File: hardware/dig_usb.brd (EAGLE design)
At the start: 146.1 x 102.6 mm, 182 parts, among them IC101 AT90USB1287-AU, IC102 74HC166D, IC103 MAX487CSA, IC202 DS1337S, IC301 LTV-356T, IC302 LTV-356T, IC303 LTV-356T, IC304 LTV-356T, IC305 LTV-356T, IC306 LTV-356T, IC307 LTV-356T, IC308 LTV-356T, K401 S202S02, K402 S202S02, K403 S202S02, K404 S202S02, K405 S202S02, K406 S202S02, K407 S202S02, K408 S202S02, Q1 16MHz, Q201 32,768kHz, T301 BCR191, T302 BCR191, T303 BCR191, T304 BCR191, T305 BCR191, T306 BCR191, T307 BCR191, T308 BCR191, X1 AKL_249-08, X102 ISP, X2 AKL_249-08, X3 AKL_230-02, X301 RIA-73-02, X302 RIA-73-02, X303 RIA-73-02, X304 RIA-73-02, X305 RIA-73-02, X4 AKL_230-02, X401 RIA-73-02, X402 RIA-73-02, X403 RIA-73-02, X404 RIA-73-02, X405 RIA-73-02, X406 RIA-73-02, X407 RIA-73-02, X5 AKL_230-04

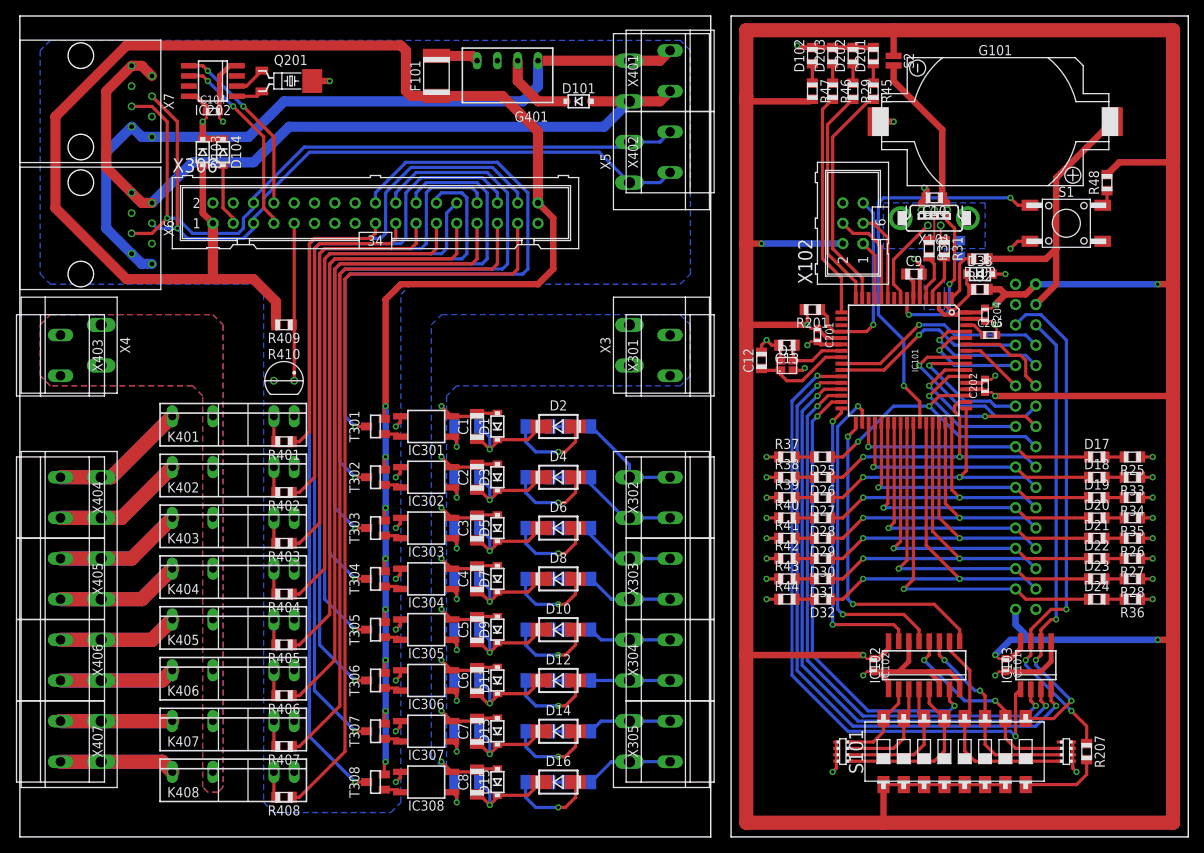
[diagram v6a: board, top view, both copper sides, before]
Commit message: dig_usb: Bauteile neu nummeriert und Plan etwas verschönert
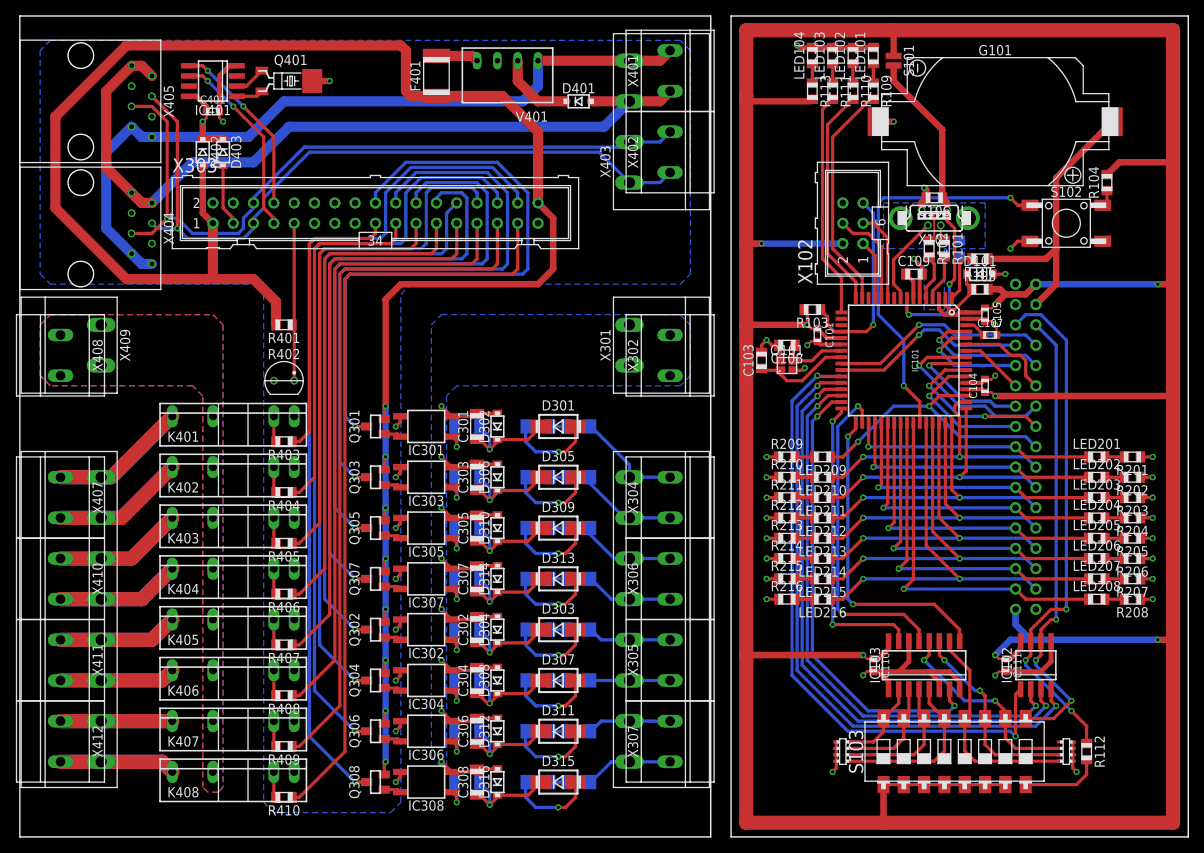
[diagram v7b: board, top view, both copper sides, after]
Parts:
- removed C11: 100nF, passiv:CHIP_0805
- removed C201, C202: 100nF, passiv:CHIP_0603
- removed D33: MMSZ5222BT1, diode:SOD123
- removed R25, R28, R36, R37: 1,5kΩ, passiv:CHIP_0805
- removed R30: 22Ω, passiv:CHIP_0805
- removed S2: (no value), schalter:JUMPER2
- removed X1: AKL_249-08, anschluss:AKL_230-08
- removed X3: AKL_230-02, anschluss:AKL_230-02
- removed X5: AKL_230-04, anschluss:AKL_230-04
- removed X6, X7: (no value), stecker:C-BMJ-0102
- added C110, C111, C401: 100nF, passiv:CHIP_0603
- added D401: SD103, diode:SOD123
- added R103: 10k, passiv:CHIP_0805
- added R106: 1MΩ, passiv:CHIP_0805
- added R107, R108: 22kΩ, widerstandsnetzwerk:1206
- added R112: 120Ω, passiv:CHIP_0805
- added S103: (no value), schalter:DIP08_SMD
- added X307, X408, X410, X411, X412: (no value), anschluss:RIA-73-02
- C102: device passiv:CHIP_0603 -> passiv:CHIP_0805
- D101: value SD103 -> MMSZ5222BT1
- D301, D303, D305, D307, D309, D311, D313, D315: value (none) -> MRA4007
- IC102: value 74HC166D -> MAX487CSA; device ic-logik:SOP16_127 -> ic-wandler:SOP08_127
- IC103: value MAX487CSA -> 74HC166D; device ic-wandler:SOP08_127 -> ic-logik:SOP16_127
- R102: value 1MΩ -> 22Ω
- R201: value 10k -> 1,5kΩ
- R207: value 120Ω -> 1,5kΩ
- R208, R209: value 22kΩ -> 1,5kΩ; device widerstandsnetzwerk:1206 -> passiv:CHIP_0805
- R401: value 470Ω -> 3,3kΩ
- R402: value 470Ω -> KTY81-210; device passiv:CHIP_0805 -> sensor:TO92
- R409: value 3,3kΩ -> 470Ω
- R410: value KTY81-210 -> 470Ω; device sensor:TO92 -> passiv:CHIP_0805
- S101: device schalter:DIP08_SMD -> schalter:JUMPER2
- X301: value RIA-73-02 -> (none); device anschluss:RIA-73-02 -> anschluss:AKL_230-02
- X302, X304, X305, X401, X402, X407: value RIA-73-02 -> (none)
- X303: value RIA-73-02 -> (none); device anschluss:RIA-73-02 -> anschluss:WS34V
- X306: device anschluss:WS34V -> anschluss:RIA-73-02
- X308: value AKL_249-08 -> (none)
- X403: value RIA-73-02 -> (none); device anschluss:RIA-73-02 -> anschluss:AKL_230-04
- X404, X405: value RIA-73-02 -> (none); device anschluss:RIA-73-02 -> stecker:C-BMJ-0102
- X406: value RIA-73-02 -> (none); device anschluss:RIA-73-02 -> anschluss:AKL_230-08
- X409: value AKL_230-02 -> (none)
- moved C104 102.4 mm to (120.7, 55.9), turned to 90 degrees
- moved S101 86.7 mm to (109.2, 96.5), turned to 270 degrees
- moved X403 76.9 mm to (76.2, 88.9), turned to 90 degrees
- moved X405 59.7 mm to (7.62, 91.4)
- moved X303 58.7 mm to (44.5, 77.5), turned to 0 degrees
- moved X306 58.7 mm to (81.3, 31.8), turned to 90 degrees
- moved D101 54.6 mm to (120.0, 69.8)
- moved C102 53.2 mm to (117.5, 73.0), flipped to the bottom
- moved R409 52.7 mm to (33.0, 10.8)
- moved R410 52.1 mm to (33.0, 4.45), turned to 180 degrees
- moved R209 50.8 mm to (95.9, 47.0), turned to 0 degrees
- moved C101 47.5 mm to (99.7, 62.2)
- moved R201 44.0 mm to (139.1, 47.0)
- moved R208 40.9 mm to (139.1, 29.2), turned to 180 degrees
- moved X404 33.8 mm to (7.62, 75.6)
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- renumbered C1 to C301, C10 to C106, C12 to C103, C13 to C108, C2 to C303, C204 to C105, C205 to C107, C3 to C305, C4 to C307, C5 to C302, C6 to C304, C7 to C306, C8 to C308, C9 to C109, D1 to D302, D10 to D303, D102 to LED104, D103 to D402, D104 to D403, D11 to D308, D12 to D307, D13 to D312, D14 to D311, D15 to D316, D16 to D315, D17 to LED201, D18 to LED202, D19 to LED203, D2 to D301, D20 to LED204, D201 to LED101, D202 to LED102, D203 to LED103, D21 to LED205, D22 to LED206, D23 to LED207, D24 to LED208, D25 to LED209, D26 to LED210, D27 to LED211, D28 to LED212, D29 to LED213, D3 to D306, D30 to LED214, D31 to LED215, D32 to LED216, D4 to D305, D5 to D310, D6 to D309, D7 to D314, D8 to D313, D9 to D304, F101 to F401, G401 to V401, IC202 to IC401, Q1 to Q101, Q201 to Q401, R1 to R302, R10 to R320, R11 to R319, R12 to R323, R13 to R304, R14 to R303, R15 to R306, R16 to R310, R17 to R309, R18 to R312, R19 to R316, R2 to R301, R20 to R315, R21 to R318, R22 to R322, R23 to R321, R24 to R324, R26 to R205, R27 to R206, R29 to R110, R3 to R305, R31 to R101, R32 to R105, R33 to R202, R34 to R203, R35 to R204, R38 to R210, R39 to R211, R4 to R308, R40 to R212, R41 to R213, R42 to R214, R43 to R215, R44 to R216, R45 to R109, R46 to R111, R47 to R113, R48 to R104, R5 to R307, R6 to R311, R7 to R314, R8 to R313, R9 to R317, S1 to S102, T301 to Q301, T302 to Q303, T303 to Q305, T304 to Q307, T305 to Q302, T306 to Q304, T307 to Q306, T308 to Q308, X2 to X308, X4 to X409
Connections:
- net !R: now also IC103.9; no longer IC102.9
- net !RESET: now also R103.1; no longer R201.1
- net +5V: now also C104.1, C110.1, C111.1, IC102.8, IC103.16, R103.2, R401.2, S101.P$1, S103.13, S103.23, S103.33, S103.43, S103.53, S103.63, S103.73, X303.1, X303.34; no longer C102.1, C201.1, C202.1, IC102.16, IC103.8, R201.2, R409.2, S101.13, S101.23, S101.33, S101.43, S101.53, S101.63, S101.73, S2.P$1, X306.1, X306.34
- net C1: now also IC103.7; no longer IC102.7
- net C2: now also IC103.15; no longer IC102.15
- net DI: now also IC103.13; no longer IC102.13
- net GND: now also C110.2, C111.2, C401.2, D101.A, IC102.5, IC103.1, IC103.14, IC103.6, IC103.8, R107.1A, R107.2A, R107.3A, R107.4A, R108.1A, R108.2A, R108.3A, R108.4A, R201.1, R207.1, R208.1, R209.1, R402.2, X303.2, X303.33, X303.4; no longer C11.2, C201.2, C202.2, D33.A, IC102.1, IC102.14, IC102.6, IC102.8, IC103.5, R208.1A, R208.2A, R208.3A, R208.4A, R209.1A, R209.2A, R209.3A, R209.4A, R25.1, R28.1, R36.1, R37.1, R410.2, X306.2, X306.33, X306.4
- net GNDIO: now also X301.P$1, X301.P$2, X302.1, X302.2; no longer X3.P$1, X3.P$2, X301.1, X301.2
- net L: now also X408.1, X408.2; no longer X403.1, X403.2
- net N$100: now also X303.30; no longer X306.30
- net N$101: now also X303.32; no longer X306.32
- net N$102: now also R201.2; no longer R25.2
- net N$108: now also R207.2; no longer R28.2
- net N$109: now also R208.2; no longer R36.2
- net N$110: now also R209.2; no longer R37.2
- net N$119: now also R102.1; no longer R30.1
- net N$120: now also R102.2; no longer R30.2
- net N$124: now also S101.P$2; no longer S2.P$2
- net N$129: now also D101.K; no longer D33.K
- net N$13: now also IC305.1; no longer IC303.1
- net N$130: now also X303.3; no longer X306.3
- net N$131: now also X303.7; no longer X306.7
- net N$132: now also X303.8; no longer X306.8
- net N$133: now also X303.6, X403.P$2, X404.P$5, X405.P$5; no longer X306.6, X5.P$2, X6.P$5, X7.P$5
- net N$134: now also X303.5, X403.P$1, X404.P$4, X405.P$4; no longer X306.5, X5.P$1, X6.P$4, X7.P$4
- net N$143: now also R106.1; no longer R102.1
- net N$146: now also R401.1, R402.1, X303.9; no longer R409.1, R410.1, X306.9
- net N$16: now also R404.2; no longer R402.2
- net N$20: now also IC102.6, S103.84; no longer IC103.6, S101.84
- net N$21: now also R106.2; no longer R102.2
- net N$22: now also IC102.7, R112.1; no longer IC103.7, R207.1
- net N$23: now also D401.K; no longer D101.K
- net N$25: now also R405.2; no longer R403.2
- net N$26: now also IC103.2, R107.1B, S103.14; no longer IC102.2, R208.1B, S101.14
- net N$27: now also IC103.3, R107.2B, S103.24; no longer IC102.3, R208.2B, S101.24
- net N$28: now also IC103.4, R107.3B, S103.34; no longer IC102.4, R208.3B, S101.34
- net N$29: now also IC103.5, R107.4B, S103.44; no longer IC102.5, R208.4B, S101.44
- net N$30: now also IC103.10, R108.1B, S103.54; no longer IC102.10, R209.1B, S101.54
- net N$31: now also IC103.11, R108.2B, S103.64; no longer IC102.11, R209.2B, S101.64
- net N$32: now also IC103.12, R108.3B, S103.74; no longer IC102.12, R209.3B, S101.74
- net N$33: now also R112.2, S103.83; no longer R207.2, S101.83
- net N$34: now also IC307.1; no longer IC304.1
- net N$37: now also R406.2; no longer R404.2
- net N$38: now also IC302.1; no longer IC305.1
- net N$42: now also R407.2; no longer R405.2
- net N$45: now also X304.1; no longer X302.1
- net N$46: now also X304.2; no longer X302.2
- net N$47: now also X306.1; no longer X303.1
- net N$48: now also X306.2; no longer X303.2
- net N$50: now also R408.2; no longer R406.2
- net N$52: now also IC307.4; no longer IC304.4
- net N$55: now also IC304.1; no longer IC306.1
- net N$56: now also X305.2; no longer X304.2
- net N$58: now also X305.1; no longer X304.1
- net N$59: now also X307.1; no longer X305.1
- net N$60: now also X307.2; no longer X305.2
- net N$61: now also R409.2; no longer R407.2
- net N$64: now also C401.1; no longer C104.1
- net N$66: now also R410.2; no longer R408.2
- net N$67: now also R403.1, X303.17; no longer R401.1, X306.17
- net N$68: now also X406.P$1, X407.1; no longer X1.P$1, X404.1
- net N$69: now also IC306.1; no longer IC307.1
- net N$70: now also IC305.4; no longer IC303.4
- net N$72: now also X406.P$2, X407.2; no longer X1.P$2, X404.2
- net N$73: now also IC303.4; no longer IC302.4
- net N$74: now also X406.P$3, X410.1; no longer X1.P$3, X405.1
- net N$76: now also X406.P$4, X410.2; no longer X1.P$4, X405.2
- net N$78: now also X406.P$5, X411.1; no longer X1.P$5, X406.1
- net N$79: now also R404.1, X303.19; no longer R402.1, X306.19
- net N$8: now also R403.2; no longer R401.2
- net N$80: now also IC302.4; no longer IC305.4
- net N$81: now also IC304.4; no longer IC306.4
- net N$82: now also X406.P$6, X411.2; no longer X1.P$6, X406.2
- net N$83: now also IC306.4; no longer IC307.4
- net N$84: now also X406.P$7, X412.1; no longer X1.P$7, X407.1
- net N$87: now also R405.1, X303.21; no longer R403.1, X306.21
- net N$88: now also R406.1, X303.23; no longer R404.1, X306.23
- net N$89: now also X406.P$8, X412.2; no longer X1.P$8, X407.2
- net N$9: now also IC303.1; no longer IC302.1
- net N$90: now also R407.1, X303.25; no longer R405.1, X306.25
- net N$91: now also R408.1, X303.27; no longer R406.1, X306.27
- net N$92: now also R409.1, X303.29; no longer R407.1, X306.29
- net N$93: now also R410.1, X303.31; no longer R408.1, X306.31
- net N$94: now also X303.18; no longer X306.18
- net N$95: now also X303.20; no longer X306.20
- net N$96: now also X303.22; no longer X306.22
- net N$97: now also X303.24; no longer X306.24
- net N$98: now also X303.26; no longer X306.26
- net N$99: now also X303.28; no longer X306.28
- net RE: now also IC102.2; no longer IC103.2
- net RXD: now also IC102.1; no longer IC103.1
- net TE: now also IC102.3; no longer IC103.3
- net TXD: now also IC102.4; no longer IC103.4
- net USHIELD: now also C102.1; no longer C11.1
- net V+: now also D401.A, X403.P$3, X404.P$1, X404.P$2, X405.P$1, X405.P$2; no longer D101.A, X5.P$3, X6.P$1, X6.P$2, X7.P$1, X7.P$2
- net V-: now also X403.P$4, X404.P$7, X404.P$8, X405.P$7, X405.P$8; no longer X5.P$4, X6.P$7, X6.P$8, X7.P$7, X7.P$8

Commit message: dig_usb: Beschriftung besser angeordnet
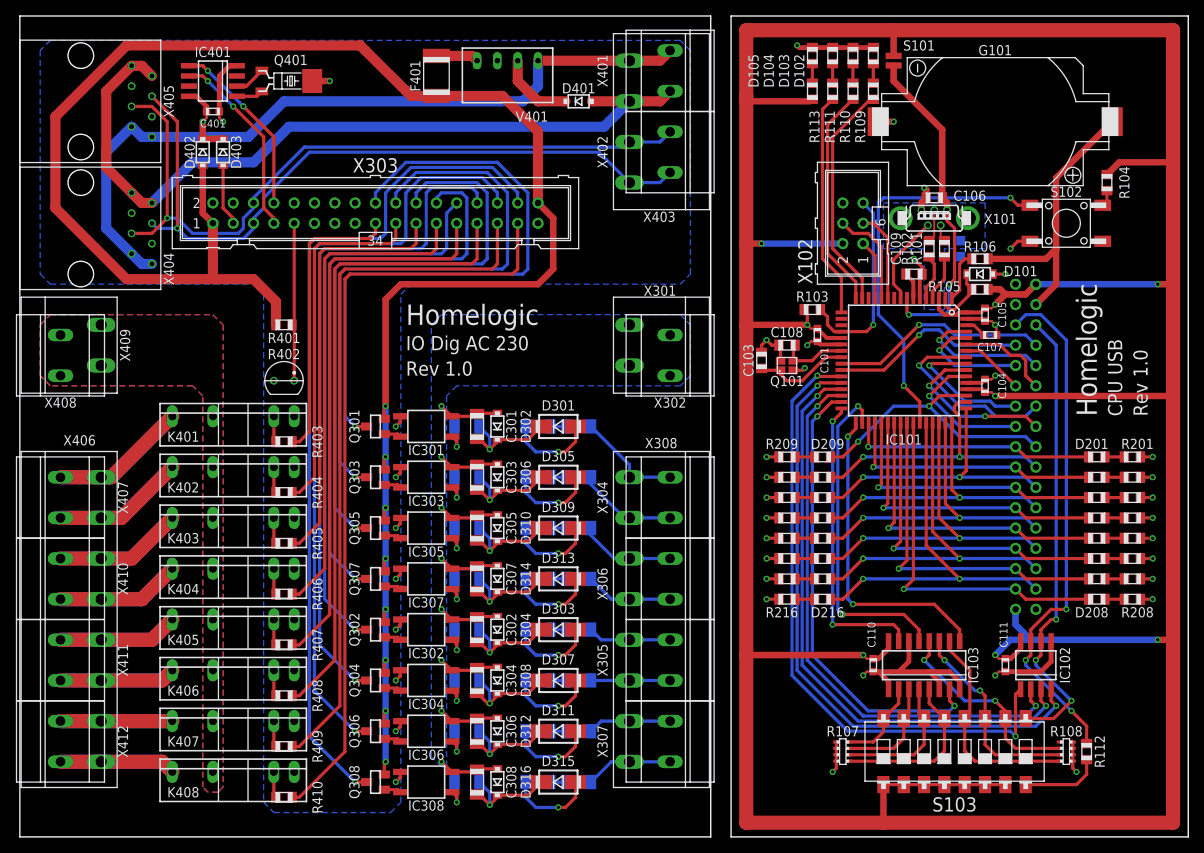
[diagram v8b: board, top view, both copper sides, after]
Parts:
- X308, X406: value (none) -> AKL_230-08
- renumbered LED101 to D102, LED102 to D103, LED103 to D104, LED104 to D105, LED201 to D201, LED202 to D202, LED203 to D203, LED204 to D204, LED205 to D205, LED206 to D206, LED207 to D207, LED208 to D208, LED209 to D209, LED210 to D210, LED211 to D211, LED212 to D212, LED213 to D213, LED214 to D214, LED215 to D215, LED216 to D216
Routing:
- net +5V: track 730.2 -> 727.2 mm
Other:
- board text added: "CPU USB"
- board text added: "Homelogic"
- board text added: "IO Dig AC 230"
- board text added: "Rev 1.0"
